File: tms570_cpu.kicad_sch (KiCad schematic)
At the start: 40 parts, among them J2 CONN_02X05, U2 TMS570LS0914PGE

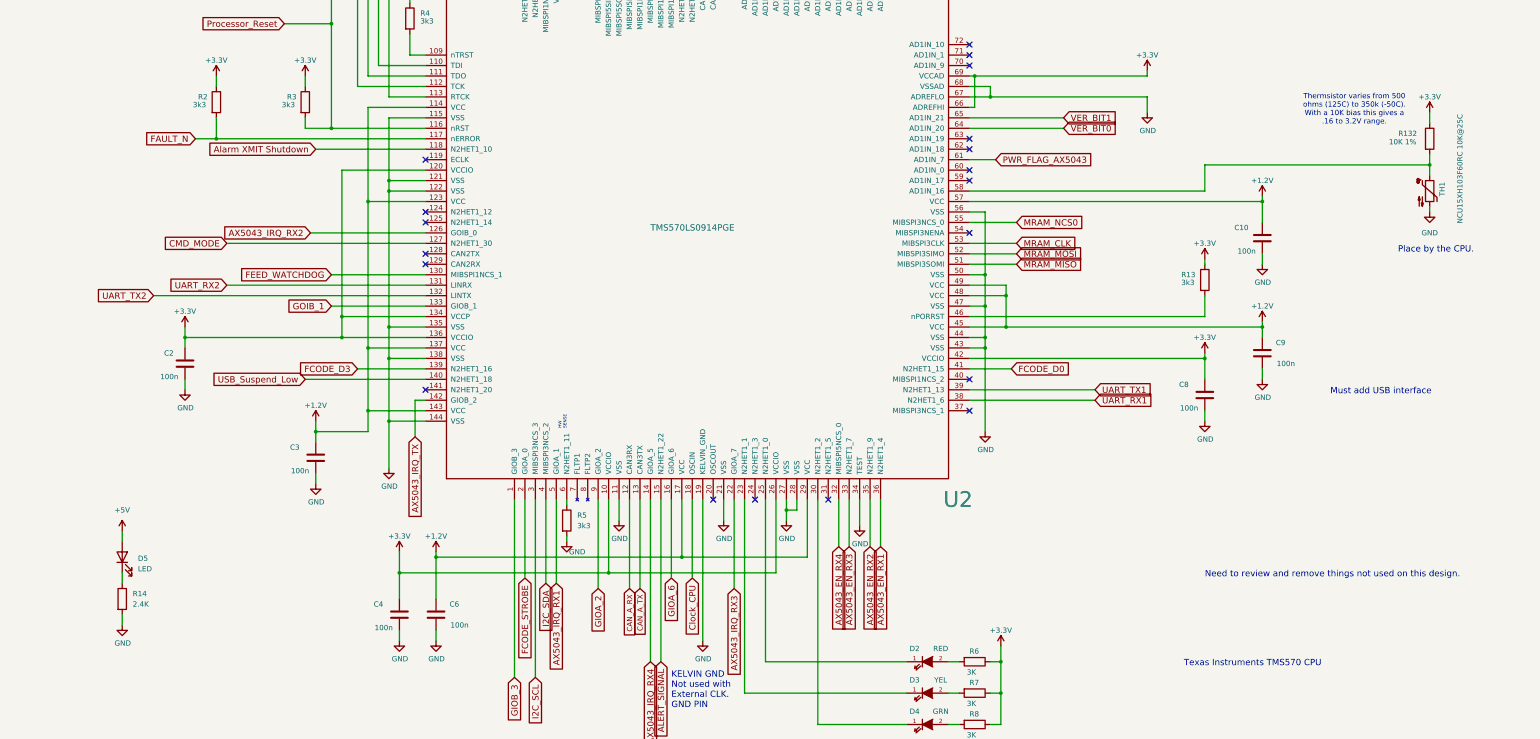
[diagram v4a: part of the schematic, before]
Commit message: Add a bunch of decoupling capacitors
Signed-off-by: Corey Minyard <corey@minyard.net>
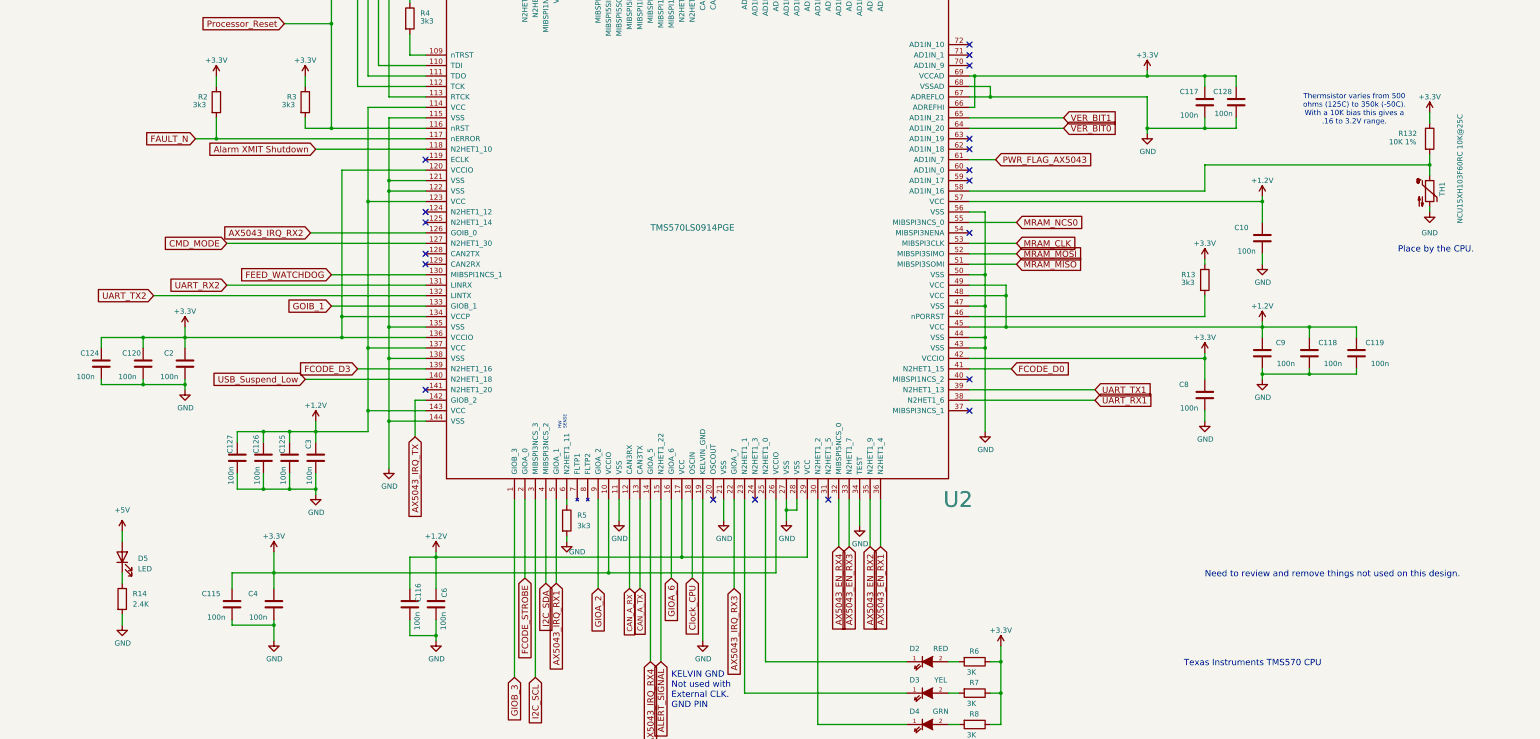
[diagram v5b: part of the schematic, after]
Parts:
- added C115, C116, C117, C118, C119, C120, C124, C125, C126, C127, C128: 100n, Capacitor_SMD:C_0603_1608Metric_Pad1.08x0.95mm_HandSolder, symbol Device:C
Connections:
- net +1.2V: now also C116.1, C118.1, C119.1, C125.1, C126.1, C127.1
- net +3.3V: now also C115.1, C117.1, C120.1, C124.1, C128.1
- net GND: now also C115.2, C116.2, C117.2, C118.2, C119.2, C120.2, C124.2, C125.2, C126.2, C127.2, C128.2
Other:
- note removed: "Must add USB interface"
- moved on the sheet: C4, C6

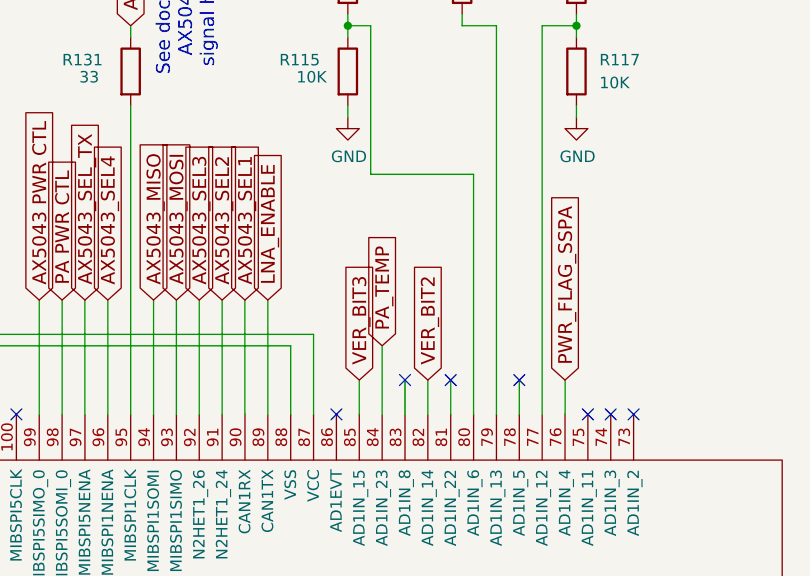
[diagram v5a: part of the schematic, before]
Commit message: Add a thermsistor for the power conversion area
Signed-off-by: Corey Minyard <corey@minyard.net>
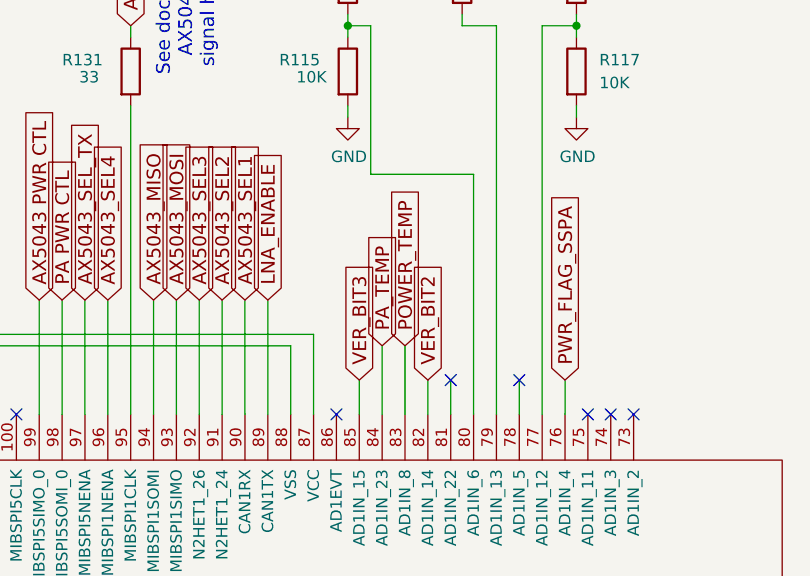
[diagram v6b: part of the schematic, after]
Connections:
- net POWER_TEMP: now reaches U2.83 (AD1IN_8)
- no-connect marks 28 -> 27
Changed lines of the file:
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@@
 		(at 149.86 137.16)
 	)
-	(no_connect
-		(at 234.95 68.58)
-	)
 	(wire
 		(pts
@@
 	(wire
 		(pts
-			(xy 234.95 68.58) (xy 234.95 72.39)
-		)
-		(stroke
-			(width 0)
-			(type default)
-		)
-	)
-	(wire
-		(pts
 			(xy 247.65 68.58) (xy 247.65 72.39)
 		)
@@
 	(wire
 		(pts
+			(xy 234.95 64.77) (xy 234.95 72.39)
+		)
+		(stroke
+			(width 0)
+			(type default)
+		)
+	)
+	(wire
+		(pts
 			(xy 196.85 59.69) (xy 196.85 72.39)
 		)
@@
 				(hide yes)
 			)
+		)
+	)
+	(global_label "POWER_TEMP"
+		(shape input)
+		(at 234.95 64.77 90)
+		(fields_autoplaced yes)
+		(effects
+			(font
+				(size 1.524 1.524)
+			)
+			(justify left)
+		)
+		(property "Intersheetrefs" "${INTERSHEET_REFS}"
+			(at 234.95 47.2412 90)
+			(effects
+				(font
+					(size 1.27 1.27)
+				)
+				(justify left)
+				(hide yes)
+			)

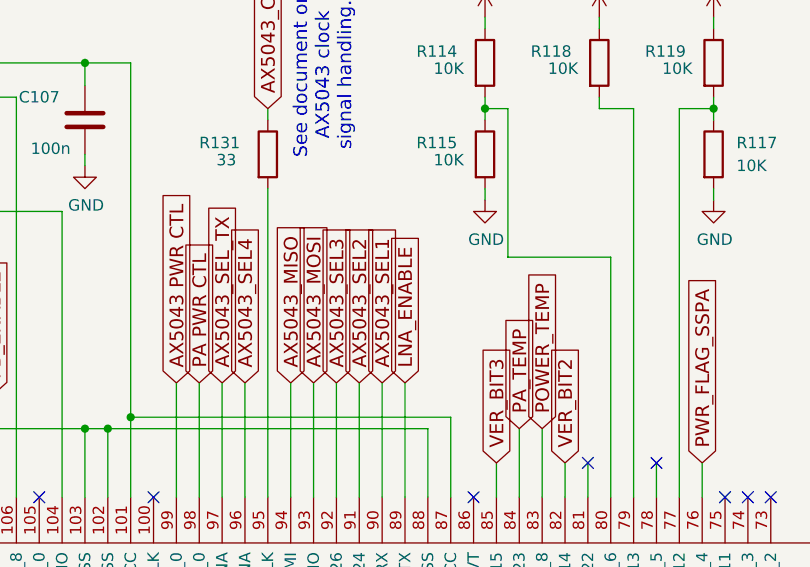
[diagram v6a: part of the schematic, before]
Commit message: Lots of cleanups around the RF shield
Signed-off-by: Corey Minyard <corey@minyard.net>
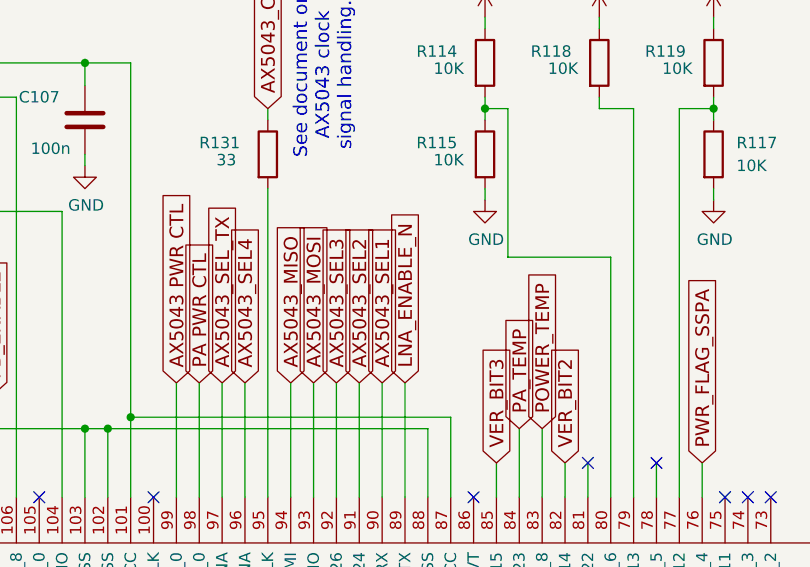
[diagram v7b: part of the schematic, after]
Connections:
- net LNA_ENABLE renamed LNA_ENABLE_N
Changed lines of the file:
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@@
 		)
 	)
-	(global_label "LNA_ENABLE"
+	(global_label "LNA_ENABLE_N"
 		(shape input)
 		(at 219.71 59.69 90)
@@
 		)
 		(property "Intersheetrefs" "${INTERSHEET_REFS}"
-			(at 219.71 43.1771 90)
+			(at 219.71 40.4194 90)
 			(effects
 				(font

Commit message: Re-annotate all parts
And get rid of the per-sheet annotation remarks.

Signed-off-by: Corey Minyard <corey@minyard.net>
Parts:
- renumbered C3 to C10, C116 to C11, C5 to C12, C6 to C13, C7 to C14, C107 to C15, C117 to C16, C8 to C17, C128 to C18, C10 to C19, C124 to C2, C9 to C20, C118 to C21, C119 to C22, C120 to C3, C2 to C4, C115 to C5, C127 to C6, C126 to C7, C4 to C8, C125 to C9, D5 to D2, D2 to D3, D3 to D4, D4 to D5, R131 to R10, R114 to R11, R115 to R12, R118 to R13, R119 to R14, R117 to R15, R6 to R16, R7 to R17, R8 to R18, R9 to R19, R14 to R2, R10 to R20, R11 to R21, R12 to R22, R13 to R23, R132 to R24, R2 to R3, R3 to R4, R136 to R5, R137 to R6, R138 to R7, R4 to R8, R5 to R9, TH1 to TH2
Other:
- note removed: "Start with 1"
